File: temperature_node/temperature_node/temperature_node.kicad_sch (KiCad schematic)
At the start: 34 parts, among them CN1 UART, J1 USB_C_Receptacle_USB2.0_16P, J2 S2B-PH-K-S, U1 SHT40-AD1B-R3, U2 MCP73831-2-OT, U3 MIC5504-3.3YM5, U4 ESP32-C3-WROOM-02

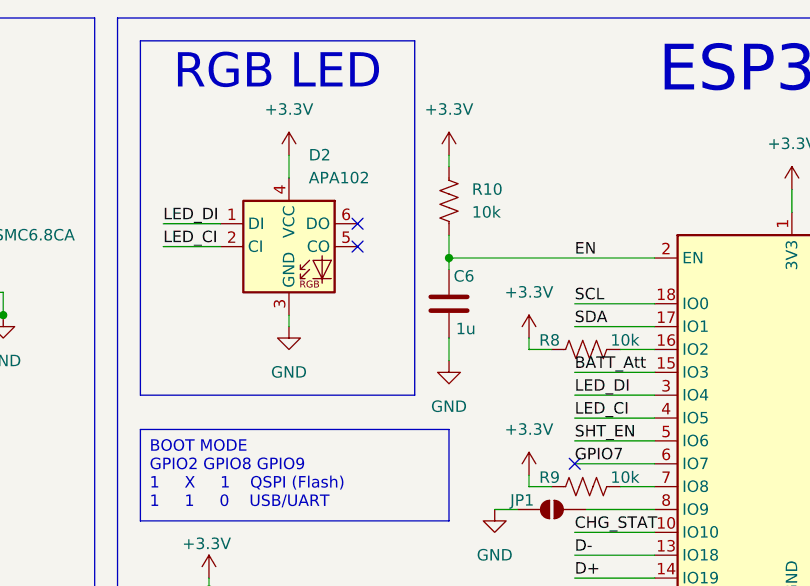
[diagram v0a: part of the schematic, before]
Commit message: Replace 5x5 mm RGB Led for a 2x2 mm
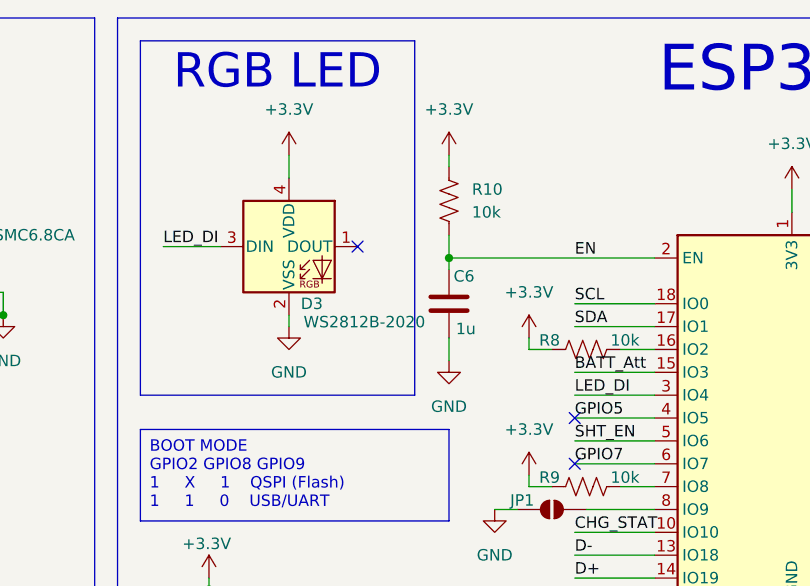
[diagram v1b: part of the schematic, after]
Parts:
- removed D2: APA102, LED_SMD:LED_RGB_5050-6, symbol LED:APA102
- added D3: WS2812B-2020, LED_SMD:LED_WS2812B-2020_PLCC4_2.0x2.0mm, symbol LED:WS2812B-2020
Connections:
- net +3.3V: now also D3.4 (VDD)
- net GND: now also D3.2 (VSS)
- net LED_DI: now also D3.3 (DIN)
- net LED_CI renamed GPIO5
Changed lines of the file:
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@@
 	)
 	(no_connect
-		(at 181.61 46.99)
-	)
-	(no_connect
 		(at 123.19 80.01)
 	)
@@
 	)
 	(no_connect
+		(at 205.74 68.58)
+	)
+	(no_connect
 		(at 205.74 73.66)
 	)
@@
 	(wire
 		(pts
-			(xy 160.02 49.53) (xy 166.37 49.53)
-		)
-		(stroke
-			(width 0)
-			(type default)
-		)
-	)
-	(wire
-		(pts
 			(xy 229.87 93.98) (xy 229.87 91.44)
 		)
@@
 	(wire
 		(pts
-			(xy 160.02 46.99) (xy 166.37 46.99)
+			(xy 160.02 49.53) (xy 166.37 49.53)
 		)
 		(stroke
@@
 	)
 	(label "LED_DI"
-		(at 160.02 46.99 0)
+		(at 160.02 49.53 0)
 		(fields_autoplaced yes)
 		(effects
@@
 		)
 	)
-	(label "LED_CI"
+	(label "GPIO5"
 		(at 205.74 68.58 0)
 		(fields_autoplaced yes)
@@
 		)
 	)
-	(label "LED_CI"
-		(at 160.02 49.53 0)
-		(fields_autoplaced yes)
-		(effects
-			(font
-				(size 1.27 1.27)
-			)
-			(justify left bottom)
-		)
-	)
 	(label "SCL"
 		(at 205.74 55.88 0)
@@
 	)
 	(symbol
+		(lib_id "LED:WS2812B-2020")
+		(at 173.99 49.53 0)
+		(unit 1)
+		(exclude_from_sim no)
+		(in_bom yes)
+		(on_board yes)
+		(dnp no)
+		(property "Reference" "D3"
+			(at 176.53 55.88 0)
+			(effects
+				(font
+					(size 1.27 1.27)
+				)
+			)
+		)
+		(property "Value" "WS2812B-2020"
+			(at 182.372 57.912 0)
+			(effects
+				(font
+					(size 1.27 1.27)
+				)
+			)
+		)
+		(property "Footprint" "LED_SMD:LED_WS2812B-2020_PLCC4_2.0x2.0mm"
+			(at 175.26 57.15 0)
+			(effects
+				(font
+					(size 1.27 1.27)
+				)
+				(justify left top)
+				(hide yes)
+			)
+		)
+		(property "Datasheet" "https://cdn-shop.adafruit.com/product-files/4684/4684_WS2812B-2020_V1.3_EN.pdf"
+			(at 176.53 59.055 0)
+			(effects
+				(font
+					(size 1.27 1.27)
+				)
+				(justify left top)
+				(hide yes)
+			)
+		)
+		(property "Description" "RGB LED with integrated controller, 2.0 x 2.0 mm, 12 mA"
+			(at 173.99 49.53 0)
+			(effects
+				(font
+					(size 1.27 1.27)
+				)
+				(hide yes)
+			)
+		)
+		(pin "1"
+		)
+		(pin "4"
+		)
+		(pin "2"
+		)
+		(pin "3"
+		)
+		(instances
+			(project ""
+				(path "/b4f604dd-c1be-4776-9f83-5b1c508883b1"
+					(reference "D3")
+					(unit 1)
+				)
+			)
+		)
+	)
+	(symbol
 		(lib_id "Connector:Conn_01x03_Pin")
 		(at 252.73 53.34 0)
@@
 					(unit 1)
 				)
-			)
-		)
-	)
-	(symbol
-		(lib_id "LED:APA102")
-		(at 173.99 49.53 0)
-		(unit 1)
-		(exclude_from_sim no)
-		(in_bom yes)
-		(on_board yes)
-		(dnp no)
-		(fields_autoplaced yes)
-		(property "Reference" "D2"
-			(at 176.1841 39.37 0)
-			(effects
-				(font
-					(size 1.27 1.27)
-				)
-				(justify left)
-			)
-		)
-		(property "Value" "APA102"
-			(at 176.1841 41.91 0)
-			(effects
-				(font
-					(size 1.27 1.27)
-				)
-				(justify left)
-			)
-		)
-		(property "Footprint" "LED_SMD:LED_RGB_5050-6"
-			(at 175.26 57.15 0)
-			(effects
-				(font
-					(size 1.27 1.27)
-				)
-				(justify left top)
-				(hide yes)
-			)
-		)
-		(property "Datasheet" "http://www.led-color.com/upload/201506/APA102%20LED.pdf"
-			(at 176.53 59.055 0)
-			(effects
-				(font
-					(size 1.27 1.27)
-				)
-				(justify left top)
-				(hide yes)
-			)
-		)
-		(property "Description" "RGB LED with integrated controller"
-			(at 173.99 49.53 0)
-			(effects
-				(font
-					(size 1.27 1.27)
-				)
-				(hide yes)
-			)
-		)
-		(pin "1"
-		)
-		(pin "2"
-		)
-		(pin "4"
-		)
-		(pin "5"
-		)
-		(pin "6"
-		)
-		(pin "3"
-		)
-		(instances
-			(project ""
-				(path "/b4f604dd-c1be-4776-9f83-5b1c508883b1"
-					(reference "D2")
-					(unit 1)
-				)

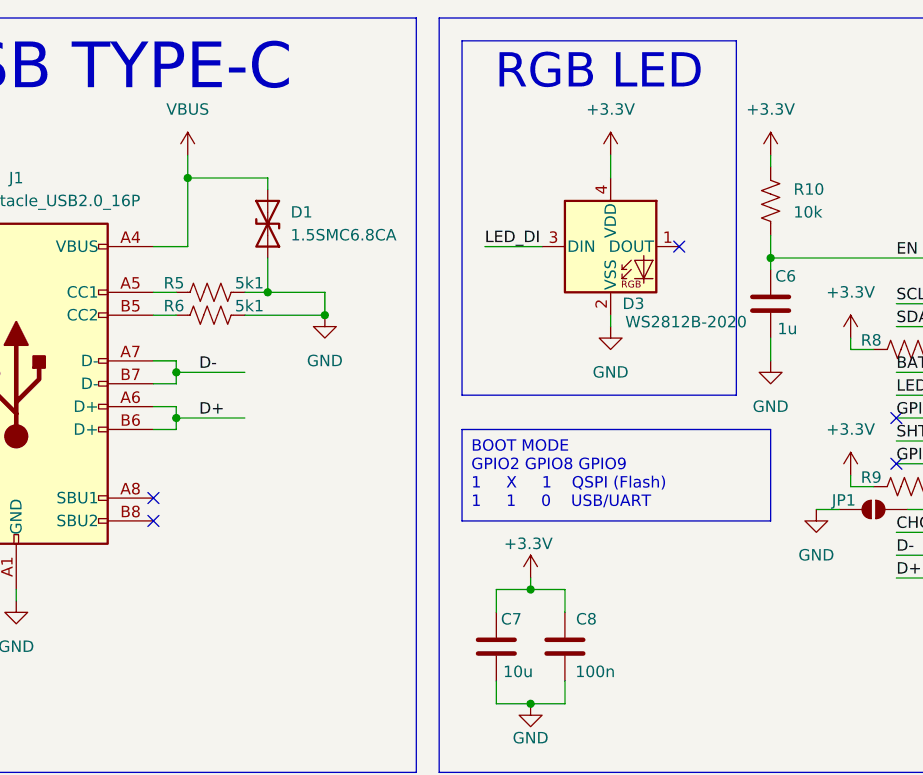
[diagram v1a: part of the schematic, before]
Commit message: Replace TVS Diode with a smaller ESD + TVS  protection for USB. Add datasheets
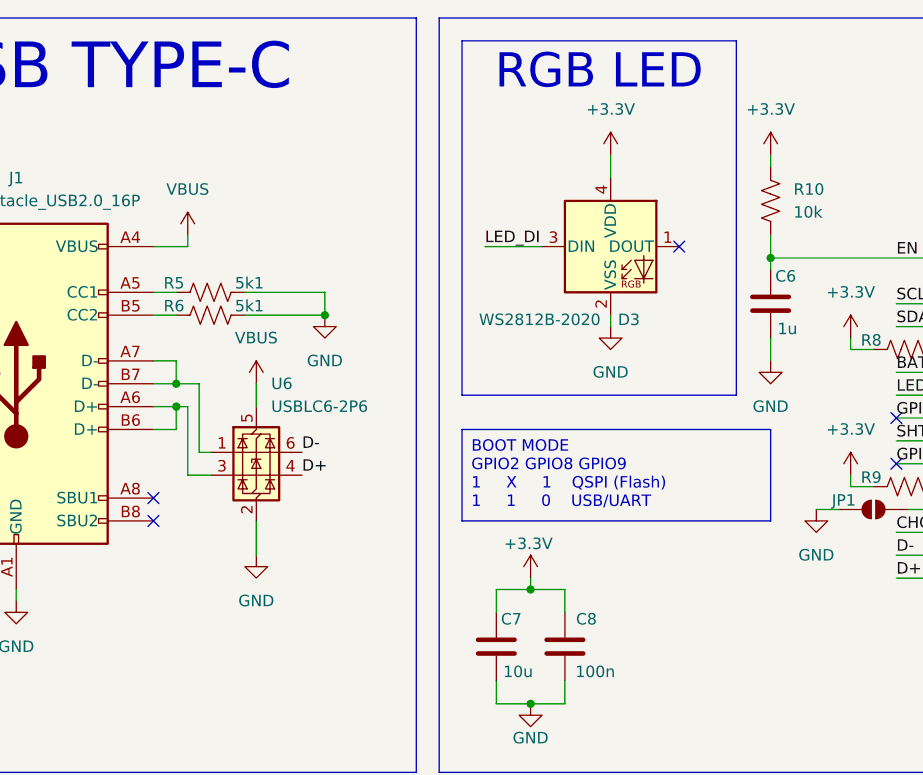
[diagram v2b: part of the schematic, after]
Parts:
- removed D1: 1.5SMC6.8CA, Diode_SMD:D_SMC, symbol Diode:1.5SMCxxCA
- added U6: USBLC6-2P6, Package_TO_SOT_SMD:SOT-666, symbol Power_Protection:USBLC6-2P6
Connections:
- net D+: now also U6.4 (I/O2); no longer J1.A6 (D+), J1.B6 (D+)
- net D-: now also U6.6 (I/O1); no longer J1.A7 (D-), J1.B7 (D-)
- net GND: now also U6.2 (GND)
- net VBUS: now also U6.5 (VBUS)
- new net: J1.A6 (D+), J1.B6 (D+), U6.3 (I/O2)
- new net: J1.A7 (D-), J1.B7 (D-), U6.1 (I/O1)

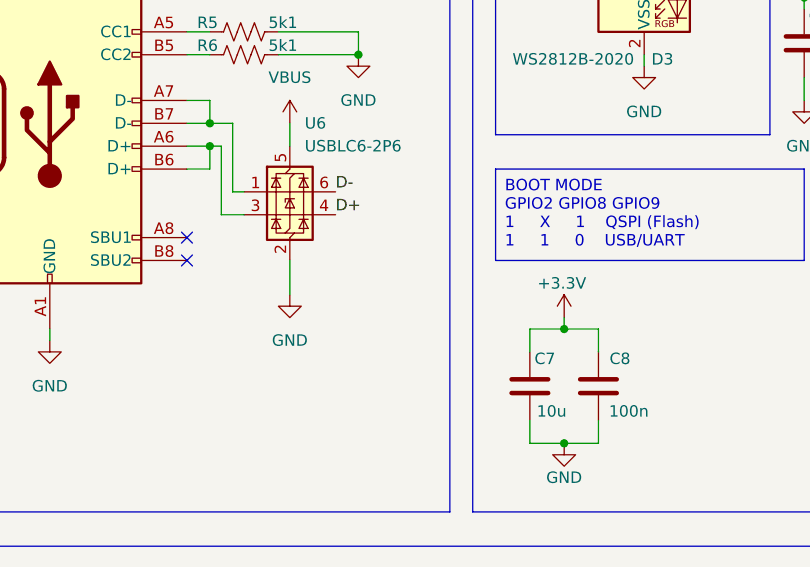
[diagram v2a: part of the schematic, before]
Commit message: Add decoupling capacitor at VBUS for ESD protection
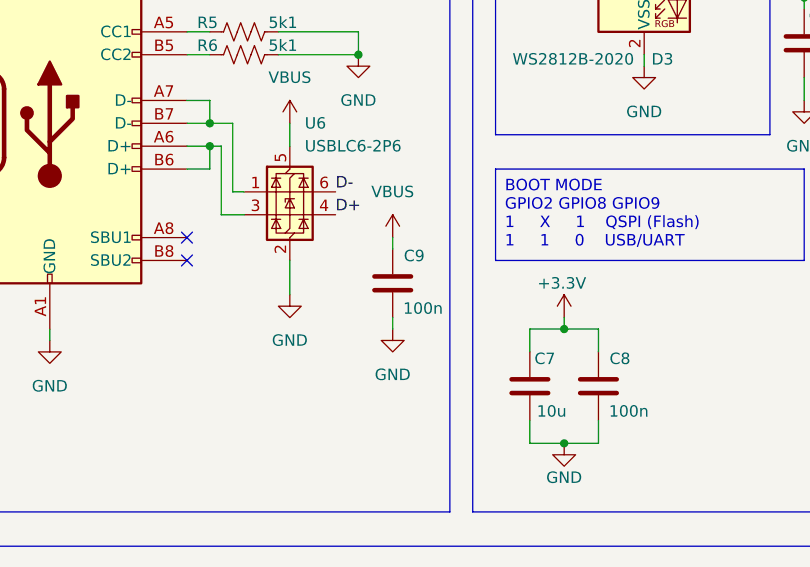
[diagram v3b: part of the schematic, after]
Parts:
- added C9: 100n, Capacitor_SMD:C_0402_1005Metric, symbol Device:C
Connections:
- net GND: now also C9.2
- net VBUS: now also C9.1
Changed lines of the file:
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@@
 	(wire
 		(pts
+			(xy 146.05 87.63) (xy 146.05 86.36)
+		)
+		(stroke
+			(width 0)
+			(type default)
+		)
+	)
+	(wire
+		(pts
 			(xy 63.5 55.88) (xy 60.96 55.88)
 		)
@@
 	(wire
 		(pts
+			(xy 146.05 77.47) (xy 146.05 78.74)
+		)
+		(stroke
+			(width 0)
+			(type default)
+		)
+	)
+	(wire
+		(pts
 			(xy 210.82 133.35) (xy 208.28 133.35)
 		)
@@
 	)
 	(symbol
+		(lib_id "power:GND")
+		(at 146.05 87.63 0)
+		(unit 1)
+		(exclude_from_sim no)
+		(in_bom yes)
+		(on_board yes)
+		(dnp no)
+		(fields_autoplaced yes)
+		(property "Reference" "#PWR035"
+			(at 146.05 93.98 0)
+			(effects
+				(font
+					(size 1.27 1.27)
+				)
+				(hide yes)
+			)
+		)
+		(property "Value" "GND"
+			(at 146.05 92.71 0)
+			(effects
+				(font
+					(size 1.27 1.27)
+				)
+			)
+		)
+		(property "Footprint" ""
+			(at 146.05 87.63 0)
+			(effects
+				(font
+					(size 1.27 1.27)
+				)
+				(hide yes)
+			)
+		)
+		(property "Datasheet" ""
+			(at 146.05 87.63 0)
+			(effects
+				(font
+					(size 1.27 1.27)
+				)
+				(hide yes)
+			)
+		)
+		(property "Description" "Power symbol creates a global label with name \"GND\" , ground"
+			(at 146.05 87.63 0)
+			(effects
+				(font
+					(size 1.27 1.27)
+				)
+				(hide yes)
+			)
+		)
+		(pin "1"
+		)
+		(instances
+			(project "temperature_node"
+				(path "/b4f604dd-c1be-4776-9f83-5b1c508883b1"
+					(reference "#PWR035")
+					(unit 1)
+				)
+			)
+		)
+	)
+	(symbol
 		(lib_id "LED:WS2812B-2020")
 		(at 173.99 49.53 0)
@@
 	)
 	(symbol
+		(lib_id "Device:C")
+		(at 146.05 82.55 0)
+		(mirror y)
+		(unit 1)
+		(exclude_from_sim no)
+		(in_bom yes)
+		(on_board yes)
+		(dnp no)
+		(property "Reference" "C9"
+			(at 149.606 79.502 0)
+			(effects
+				(font
+					(size 1.27 1.27)
+				)
+				(justify left)
+			)
+		)
+		(property "Value" "100n"
+			(at 151.638 85.344 0)
+			(effects
+				(font
+					(size 1.27 1.27)
+				)
+				(justify left)
+			)
+		)
+		(property "Footprint" "Capacitor_SMD:C_0402_1005Metric"
+			(at 145.0848 86.36 0)
+			(effects
+				(font
+					(size 1.27 1.27)
+				)
+				(hide yes)
+			)
+		)
+		(property "Datasheet" "~"
+			(at 146.05 82.55 0)
+			(effects
+				(font
+					(size 1.27 1.27)
+				)
+				(hide yes)
+			)
+		)
+		(property "Description" "Unpolarized capacitor"
+			(at 146.05 82.55 0)
+			(effects
+				(font
+					(size 1.27 1.27)
+				)
+				(hide yes)
+			)
+		)
+		(pin "2"
+		)
+		(pin "1"
+		)
+		(instances
+			(project "temperature_node"
+				(path "/b4f604dd-c1be-4776-9f83-5b1c508883b1"
+					(reference "C9")
+					(unit 1)
+				)
+			)
+		)
+	)
+	(symbol
 		(lib_id "power:GND")
 		(at 60.96 74.93 0)
@@
 					(unit 1)
 				)
+			)
+		)
+	)
+	(symbol
+		(lib_id "power:VBUS")
+		(at 146.05 77.47 0)
+		(unit 1)
+		(exclude_from_sim no)
+		(in_bom yes)
+		(on_board yes)
+		(dnp no)
+		(property "Reference" "#PWR034"
+			(at 146.05 81.28 0)
+			(effects
+				(font
+					(size 1.27 1.27)
+				)
+				(hide yes)
+			)
+		)
+		(property "Value" "VBUS"
+			(at 146.05 72.39 0)
+			(effects
+				(font
+					(size 1.27 1.27)
+				)
+			)
+		)
+		(property "Footprint" ""
+			(at 146.05 77.47 0)
+			(effects
+				(font
+					(size 1.27 1.27)
+				)
+				(hide yes)
+			)
+		)
+		(property "Datasheet" ""
+			(at 146.05 77.47 0)
+			(effects
+				(font
+					(size 1.27 1.27)
+				)
+				(hide yes)
+			)
+		)
+		(property "Description" "Power symbol creates a global label with name \"VBUS\""
+			(at 146.05 77.47 0)
+			(effects
+				(font
+					(size 1.27 1.27)
+				)
+				(hide yes)
+			)
+		)
+		(pin "1"
+		)
+		(instances
+			(project "temperature_node"
+				(path "/b4f604dd-c1be-4776-9f83-5b1c508883b1"
+					(reference "#PWR034")
+					(unit 1)
+				)
